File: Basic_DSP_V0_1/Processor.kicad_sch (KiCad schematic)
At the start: 40 parts, among them J12 Conn_ARM_SWD_TagConnect_TC2030, Q1 AO3400A, Q2 AO3400A, Q3 AO3400A, U1 STM32F415RGTx, Y1 ABM8G-24.000MHZ-18-D2Y-T3

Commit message: Minor layout work
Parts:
- removed C64: 100n, Capacitor_SMD:C_0603_1608Metric_Pad1.08x0.95mm_HandSolder, symbol Device:C_Small
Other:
- moved on the sheet: C65
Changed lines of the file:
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@@
 	)
 	(junction
-		(at 275.59 80.01)
-		(diameter 0)
-		(color 0 0 0 0)
-	)
-	(junction
 		(at 346.71 67.31)
 		(diameter 0)
@@
 	)
 	(junction
-		(at 275.59 67.31)
-		(diameter 0)
-		(color 0 0 0 0)
-	)
-	(junction
 		(at 365.76 138.43)
 		(diameter 0)
@@
 	(wire
 		(pts
-			(xy 287.02 76.2) (xy 287.02 80.01)
-		)
-		(stroke
-			(width 0)
-			(type default)
-		)
-	)
-	(wire
-		(pts
 			(xy 163.83 128.27) (xy 175.26 128.27)
 		)
@@
 	(wire
 		(pts
-			(xy 287.02 71.12) (xy 287.02 67.31)
-		)
-		(stroke
-			(width 0)
-			(type default)
-		)
-	)
-	(wire
-		(pts
 			(xy 377.19 76.2) (xy 377.19 80.01)
 		)
@@
 	(wire
 		(pts
-			(xy 287.02 80.01) (xy 275.59 80.01)
-		)
-		(stroke
-			(width 0)
-			(type default)
-		)
-	)
-	(wire
-		(pts
 			(xy 377.19 67.31) (xy 377.19 71.12)
 		)
@@
 	(wire
 		(pts
-			(xy 275.59 76.2) (xy 275.59 80.01)
+			(xy 275.59 76.2) (xy 275.59 82.55)
 		)
 		(stroke
@@
 	(wire
 		(pts
-			(xy 275.59 67.31) (xy 287.02 67.31)
-		)
-		(stroke
-			(width 0)
-			(type default)
-		)
-	)
-	(wire
-		(pts
 			(xy 101.6 59.69) (xy 128.27 59.69)
 		)
@@
 	(wire
 		(pts
-			(xy 275.59 67.31) (xy 275.59 71.12)
+			(xy 275.59 66.04) (xy 275.59 71.12)
 		)
 		(stroke
@@
 	(wire
 		(pts
-			(xy 275.59 66.04) (xy 275.59 67.31)
-		)
-		(stroke
-			(width 0)
-			(type default)
-		)
-	)
-	(wire
-		(pts
 			(xy 74.93 59.69) (xy 96.52 59.69)
 		)
@@
 	(wire
 		(pts
-			(xy 275.59 80.01) (xy 275.59 82.55)
-		)
-		(stroke
-			(width 0)
-			(type default)
-		)
-	)
-	(wire
-		(pts
 			(xy 106.68 123.19) (xy 106.68 133.35)
 		)
@@
 	(symbol
 		(lib_id "Device:C_Small")
-		(at 287.02 73.66 0)
+		(at 275.59 73.66 0)
 		(unit 1)
 		(exclude_from_sim no)
@@
 		(fields_autoplaced yes)
 		(property "Reference" "C65"
-			(at 289.56 72.3962 0)
+			(at 278.13 72.3962 0)
 			(effects
 				(font
@@
 		)
 		(property "Value" "2u2"
-			(at 289.56 74.9362 0)
+			(at 278.13 74.9362 0)
 			(effects
 				(font
@@
 		)
 		(property "Footprint" "Capacitor_SMD:C_0603_1608Metric_Pad1.08x0.95mm_HandSolder"
-			(at 287.02 73.66 0)
+			(at 275.59 73.66 0)
 			(effects
 				(font
@@
 		)
 		(property "Datasheet" "~"
-			(at 287.02 73.66 0)
+			(at 275.59 73.66 0)
 			(effects
 				(font
@@
 		)
 		(property "Description" "Unpolarized capacitor, small symbol"
-			(at 287.02 73.66 0)
+			(at 275.59 73.66 0)
 			(effects
 				(font
@@
 		)
 		(property "MF" "FH (Guangdong Fenghua Advanced Tech) "
-			(at 287.02 73.66 0)
+			(at 275.59 73.66 0)
 			(effects
 				(font
@@
 		)
 		(property "MPN" "0603B225K250NT"
-			(at 287.02 73.66 0)
+			(at 275.59 73.66 0)
 			(effects
 				(font
@@
 		)
 		(property "OC_MOUSER" ""
-			(at 287.02 73.66 0)
+			(at 275.59 73.66 0)
 			(effects
 				(font
@@
 		)
 		(property "OC_LCSC" "C99228"
-			(at 287.02 73.66 0)
+			(at 275.59 73.66 0)
 			(effects
 				(font
@@
 		)
 		(property "Voltage" "25V"
-			(at 287.02 73.66 0)
+			(at 275.59 73.66 0)
 			(effects
 				(font
@@
 					(unit 1)
 				)
-			)
-		)
-	)
-	(symbol
-		(lib_id "Device:C_Small")
-		(at 275.59 73.66 0)
-		(unit 1)
-		(exclude_from_sim no)
-		(in_bom yes)
-		(on_board yes)
-		(dnp no)
-		(property "Reference" "C64"
-			(at 278.13 72.3962 0)
-			(effects
-				(font
-					(size 1.27 1.27)
-				)
-				(justify left)
-			)
-		)
-		(property "Value" "100n"
-			(at 277.876 74.422 0)
-			(effects
-				(font
-					(size 1.27 1.27)
-				)
-				(justify left)
-			)
-		)
-		(property "Footprint" "Capacitor_SMD:C_0603_1608Metric_Pad1.08x0.95mm_HandSolder"
-			(at 275.59 73.66 0)
-			(effects
-				(font
-					(size 1.27 1.27)
-				)
-				(hide yes)
-			)
-		)
-		(property "Datasheet" "~"
-			(at 275.59 73.66 0)
-			(effects
-				(font
-					(size 1.27 1.27)
-				)
-				(hide yes)
-			)
-		)
-		(property "Description" "Unpolarized capacitor, small symbol"
-			(at 275.59 73.66 0)
-			(effects
-				(font
-					(size 1.27 1.27)
-				)
-				(hide yes)
-			)
-		)
-		(property "MPN" "0603B104M250NT"
-			(at 275.59 73.66 0)
-			(effects
-				(font
-					(size 1.27 1.27)
-				)
-				(hide yes)
-			)
-		)
-		(property "MF" "FH (Guangdong Fenghua Advanced Tech) "
-			(at 275.59 73.66 0)
-			(effects
-				(font
-					(size 1.27 1.27)
-				)
-				(hide yes)
-			)
-		)
-		(property "OC_MOUSER" "963-BAST105SB7104KF"
-			(at 275.59 73.66 0)
-			(effects
-				(font
-					(size 1.27 1.27)
-				)
-				(hide yes)
-			)
-		)
-		(property "Voltage" "25V"
-			(at 279.908 76.708 0)
-			(effects
-				(font
-					(size 1.27 1.27)
-				)
-			)
-		)
-		(property "OC_LCSC" "C336628"
-			(at 275.59 73.66 0)
-			(effects
-				(font
-					(size 1.27 1.27)
-				)
-				(hide yes)
-			)
-		)
-		(pin "2"
-		)
-		(pin "1"
-		)
-		(instances
-			(project "Basic_DSP_V0_1"
-				(path "/b632011b-bebd-450c-b21c-a571983f756a/e7dbc969-ba2c-45c9-9dd2-cc5d15b1c61e"
-					(reference "C64")
-					(unit 1)
-				)

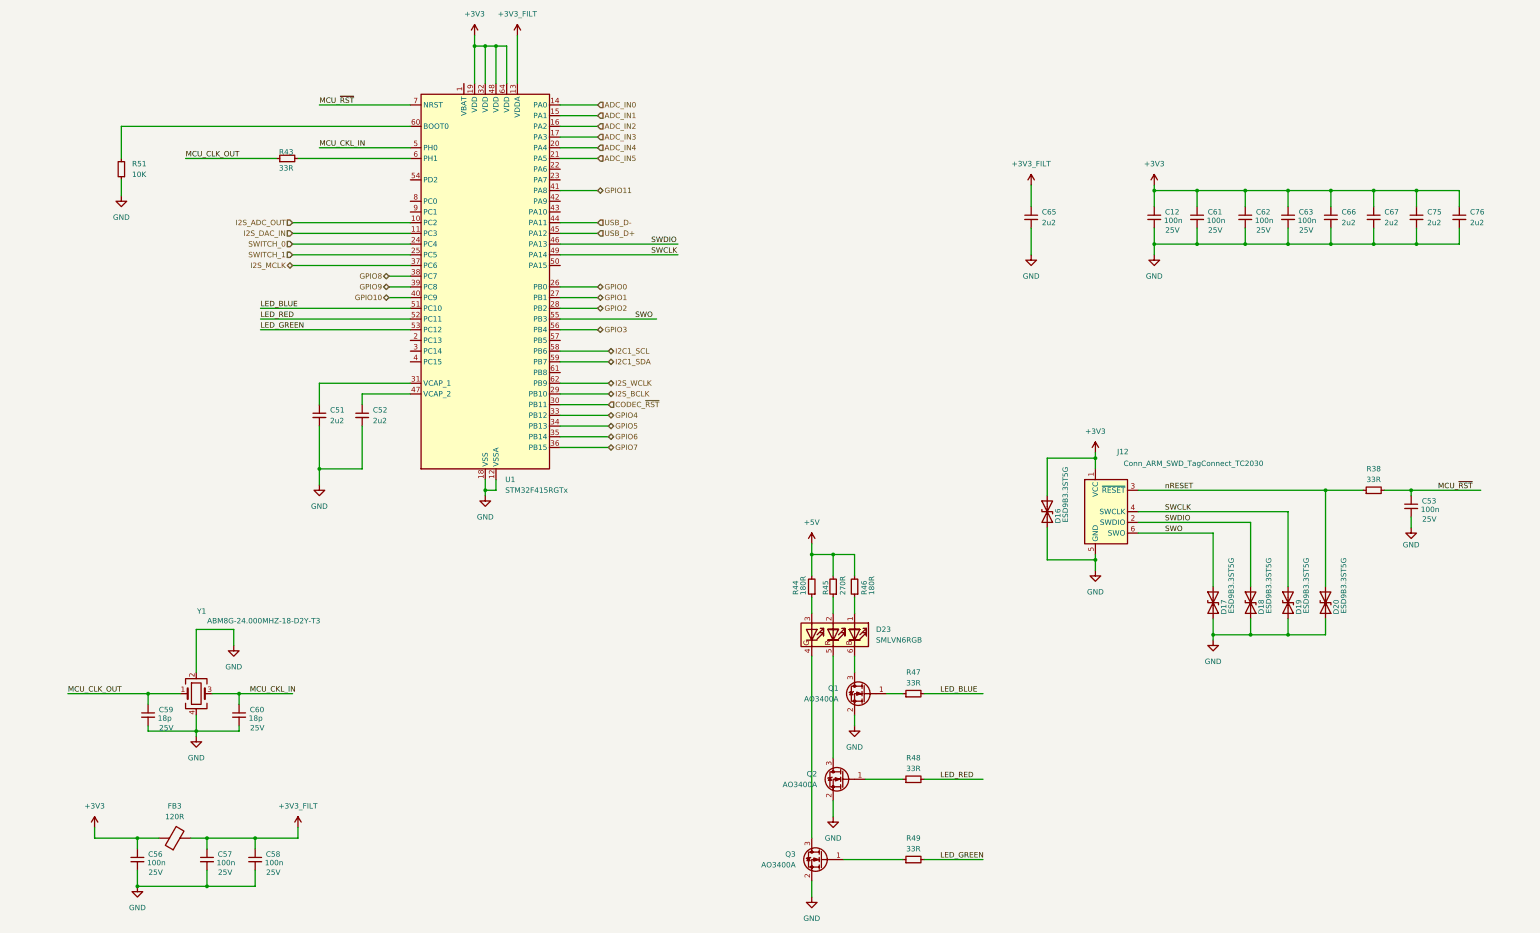
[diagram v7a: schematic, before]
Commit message: Layout and removal of PDN ferrites
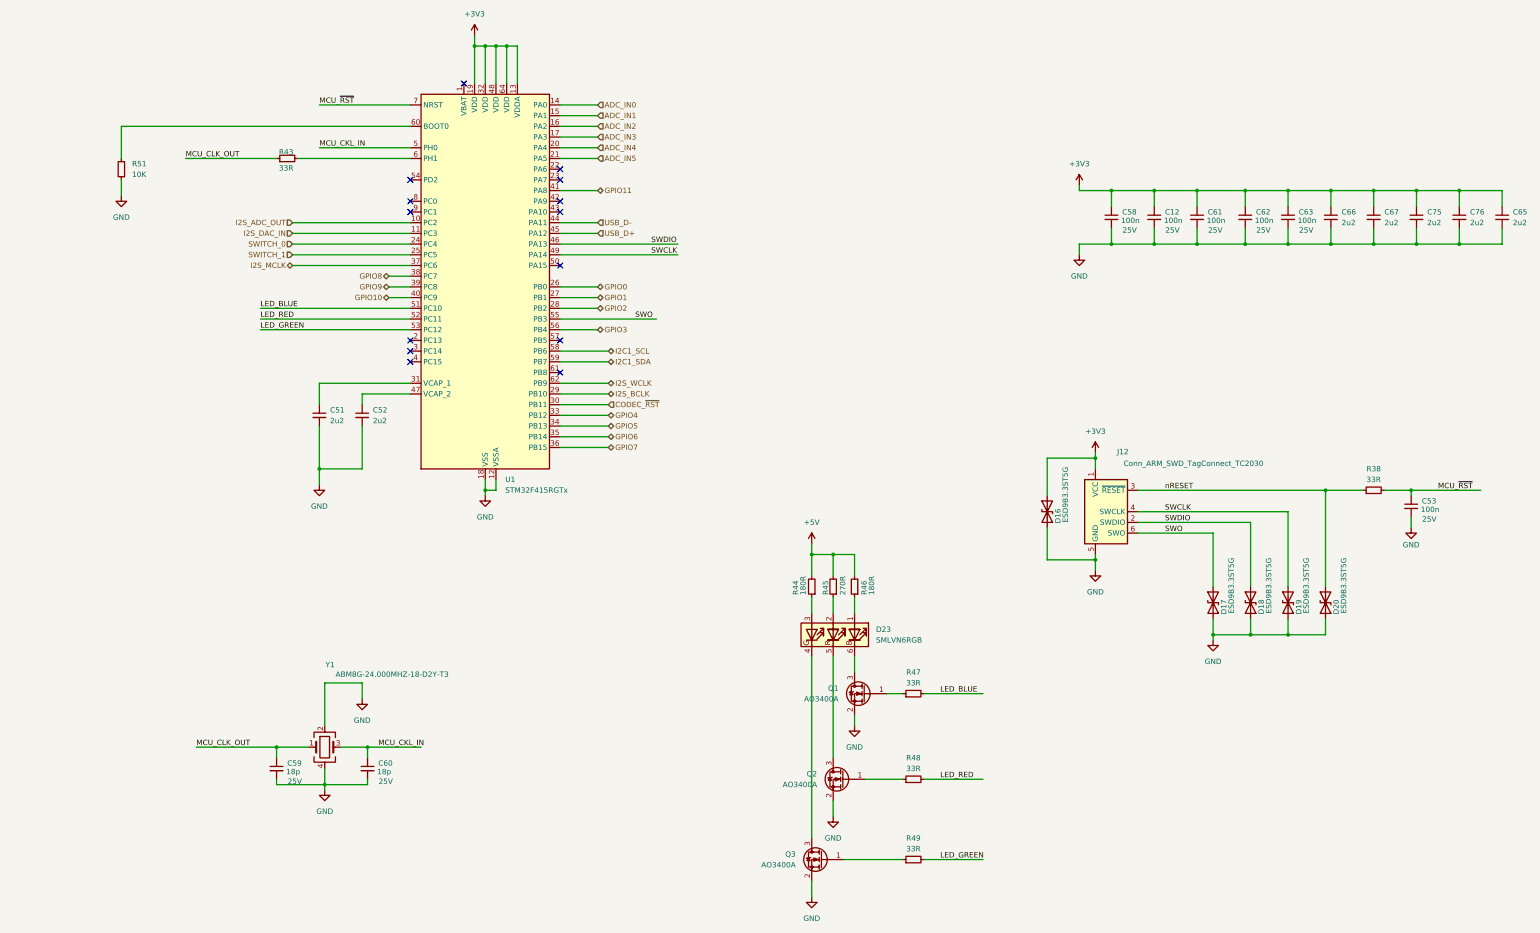
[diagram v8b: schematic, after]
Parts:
- removed C56, C57: 100n, Capacitor_SMD:C_0603_1608Metric_Pad1.08x0.95mm_HandSolder, symbol Device:C_Small
- removed FB3: 120R, Inductor_SMD:L_0603_1608Metric, symbol Device:FerriteBead
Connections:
- net +3V3_FILT is gone; now on net +3V3: C58.1, C65.1, U1.13 (VDDA)
- no-connect marks 0 -> 14
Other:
- moved on the sheet: C58, C59, C60, C65, Y1
